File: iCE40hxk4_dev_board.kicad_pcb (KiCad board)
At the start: 4 copper layers, 67 x 161.8 mm, 383 parts, among them J1001 Testpoint, J1002 Testpoint, J1003 Testpoint, J1004 Testpoint, J1005 USB_EXT, J101 CONN_01X02, J102 Jack Estereo, J103 CONN_COAXIAL, J104 CONN_COAXIAL, J105 MountingHole, J106 MountingHole, J107 MountingHole, J108 MountingHole, J1101 CONN_01X25, J202 USB_OTG, J401 Testpoint, J402 Testpoint, J403 Testpoint, J404 Testpoint, J405 Testpoint, J406 Testpoint, J501 Testpoint, J502 Testpoint, J601 CONN_01X02, J602 CONN_01X02, J603 Testpoint, J604 Testpoint, J605 Testpoint, J701 Testpoint, J702 Testpoint, J705 Testpoint, J706 Testpoint, J801 Testpoint, J802 Testpoint, J803 Testpoint, J804 Testpoint, J805 Testpoint, J806 Testpoint, J807 Testpoint, J808 Testpoint, J809 Testpoint, J810 Testpoint, SW1101 SW_Push, U1001 ADC1175, U1002 ADC1175, U1101 MIC7300, U1102 MIC7300, U1103 MCP4716, U1104 MCP4716, U1105 MIC7300, U1106 MIC7300, U201 MIC2005A-2YM5, U203 93LC56BT-I/OT, U204 MIC5355-S4YMME, U205 FT2232H, U301 iCE40-HX4K-TQ144, U302 FLASH 2Mb, U501 AS4C1M16S-7TCN, U701 CPC1017N, U702 CPC1017N, U703 CD4051BM96, U704 CD4051BM96, U801 CD4051BM96, U802 CD4051BM96, U803 CLC4007, U901 LM2776DBVR, U902 TCR2EF13,LM, U903 MIC5270

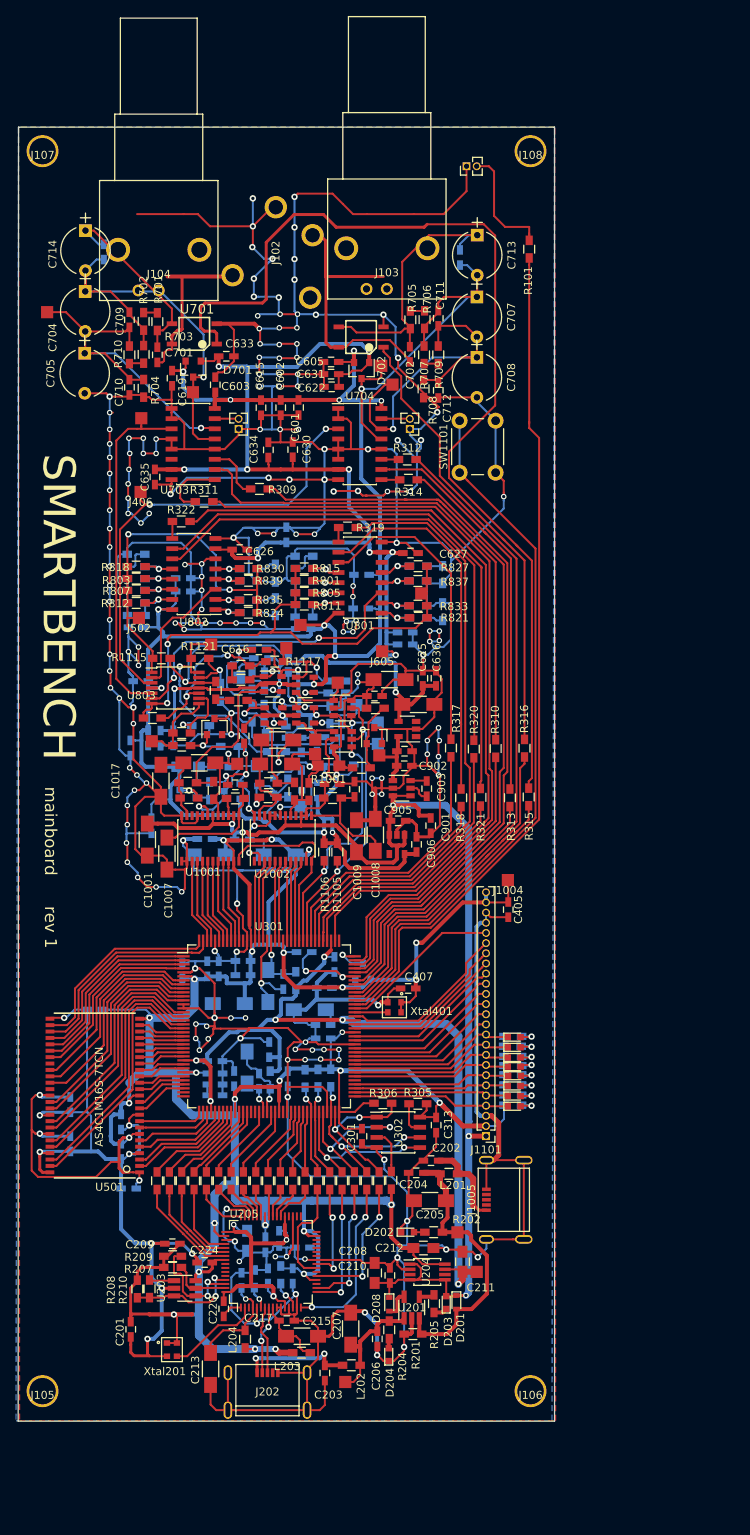
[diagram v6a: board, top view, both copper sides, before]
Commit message: Corrected routing in analogue part of board
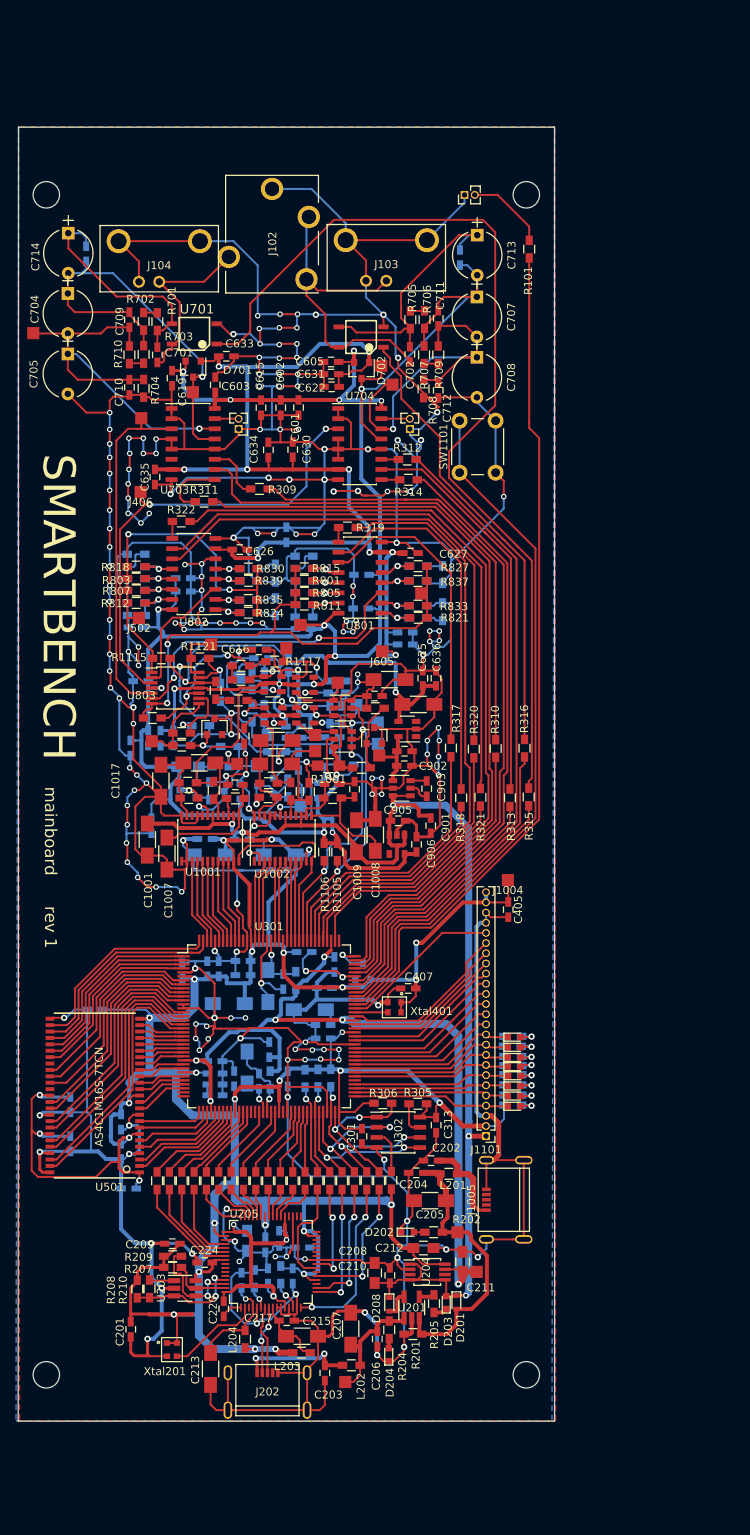
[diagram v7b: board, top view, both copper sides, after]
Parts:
- moved J108 5.61 mm to (151.3, 37.6)
- moved J107 5.17 mm to (90.9, 37.2)
- moved J101 3.60 mm to (143.3, 37.5)
- moved J404 3.14 mm to (89.4, 54.8)
- moved J102 2.34 mm to (119.2, 36.8)
- moved C703 2.22 mm to (96.0, 44.9)
- moved C704 2.19 mm to (93.7, 49.8)
- moved C714 2.17 mm to (93.8, 42.3)
- moved C705 2.11 mm to (93.7, 57.4)
- moved J104 1.08 mm to (105.1, 45.8)
- moved J103 1.02 mm to (133.5, 45.7)
- moved J803 0.59 mm to (124.6, 105.0)
- moved R1006 0.46 mm to (121.6, 112.0)
- moved J701 0.37 mm to (124.6, 107.0)
- moved R1012 0.36 mm to (122.5, 108.3)
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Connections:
- J101 pad 1: Net-(J101-Pad1) -> GND
- J101 pad 2: Net-(J101-Pad1) -> Net-(J101-Pad2)
- R101 pad 2: Net-(J101-Pad1) -> Net-(J101-Pad2)
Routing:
- net Net-(J101-Pad1): track 26.4 -> 0.00 mm
- net /CHA: track 45.1 -> 23.2 mm
- net /Analog front end/ATTENUATION/CHA_ATT_20dB: track 43.5 -> 55.1 mm
- net Net-(J101-Pad2): track 0.00 -> 10.2 mm
- net /Analog front end/ATTENUATION/CHA_DC_COUPLING: track 129.5 -> 120.5 mm
- net /Analog front end/ATTENUATION/CHA_ATT_40dB: track 46.1 -> 52.3 mm
- net /CHB: track 36.1 -> 40.2 mm
- net Net-(C701-Pad1): track 24.5 -> 28.0 mm
- net GND: track 1530.3 -> 1532.8 mm, vias 199 -> 188
- net Net-(D1001-Pad1): track 11.5 -> 9.29 mm
- net Net-(C702-Pad1): track 34.6 -> 32.5 mm
- net /Analog front end/CHB_DAC: track 6.59 -> 5.72 mm

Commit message: Fab files
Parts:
- moved J1005 2.00 mm to (149.4, 163.1)
- moved J106 1.90 mm to (150.9, 188.8)
- moved J105 1.85 mm to (90.9, 188.8)
- moved J107 0.79 mm to (91.4, 37.8)
- moved J108 0.67 mm to (150.7, 37.9)
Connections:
- J1005 pad 2: Net-(J1005-Pad2) -> (no net)
- J1005 pad 3: Net-(J1005-Pad3) -> (no net)
- J1005 pad 4: Net-(J1005-Pad4) -> (no net)
- J101 pad 1: GND -> Net-(J101-Pad1)
- J101 pad 2: Net-(J101-Pad2) -> Net-(J101-Pad1)
- J202 pad 4: Net-(J202-Pad4) -> (no net)
- R101 pad 2: Net-(J101-Pad2) -> Net-(J101-Pad1)
- U1001 pad 16: Net-(U1001-Pad16) -> (no net)
- U1001 pad 22: Net-(U1001-Pad22) -> (no net)
- U1002 pad 16: Net-(U1002-Pad16) -> (no net)
- U1002 pad 22: Net-(U1002-Pad22) -> (no net)
- U205 pad 19: Net-(U205-Pad19) -> (no net)
- U205 pad 22: Net-(U205-Pad22) -> (no net)
- U205 pad 26: Net-(U205-Pad26) -> (no net)
- U205 pad 27: Net-(U205-Pad27) -> (no net)
- U205 pad 28: Net-(U205-Pad28) -> (no net)
- U205 pad 29: Net-(U205-Pad29) -> (no net)
- U205 pad 3: Net-(U205-Pad3) -> (no net)
- U205 pad 30: Net-(U205-Pad30) -> (no net)
- U205 pad 32: Net-(U205-Pad32) -> (no net)
- U205 pad 33: Net-(U205-Pad33) -> (no net)
- U205 pad 34: Net-(U205-Pad34) -> (no net)
- U205 pad 36: Net-(U205-Pad36) -> (no net)
- U205 pad 57: Net-(U205-Pad57) -> (no net)
- U205 pad 58: Net-(U205-Pad58) -> (no net)
- U205 pad 59: Net-(U205-Pad59) -> (no net)
- U205 pad 60: Net-(U205-Pad60) -> (no net)
- U301 pad 109: Net-(U301-Pad109) -> (no net)
- U301 pad 133: Net-(U301-Pad133) -> (no net)
- U301 pad 35: Net-(U301-Pad35) -> (no net)
- U301 pad 36: Net-(U301-Pad36) -> (no net)
- U301 pad 50: Net-(U301-Pad50) -> (no net)
- U301 pad 51: Net-(U301-Pad51) -> (no net)
- U301 pad 58: Net-(U301-Pad58) -> (no net)
- U301 pad 77: Net-(U301-Pad77) -> (no net)
- U501 pad 33: Net-(U501-Pad33) -> (no net)
- U501 pad 37: Net-(U501-Pad37) -> (no net)
- U902 pad 4: Net-(U902-Pad4) -> (no net)
- U903 pad 1: Net-(U903-Pad1) -> (no net)
- U903 pad 3: Net-(U903-Pad3) -> (no net)
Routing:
- net GND: track 1532.8 -> 1551.8 mm, vias 188 -> 197
- net Net-(J101-Pad1): track 0.00 -> 10.7 mm
- net Net-(J101-Pad2): track 10.2 -> 0.00 mm
- net +3V3: track 507.6 -> 504.3 mm
- net Net-(C202-Pad1): track 11.1 -> 13.3 mm
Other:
- board size 67 x 161.8 mm -> 67 x 157 mm
